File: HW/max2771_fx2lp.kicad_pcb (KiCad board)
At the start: 4 copper layers, 30.7 x 34.2 mm, 70 parts, among them J1 SMA-ANG, J2 SMA-ANG, J3 Screw_Terminal_01x02, J4 SMA-ANG, J5 Conn_01x05_Pin, P1 Conn_02x10_Odd_Even, P2 Conn_02x10_Odd_Even, U1 MAX2771, U2 MAX2771

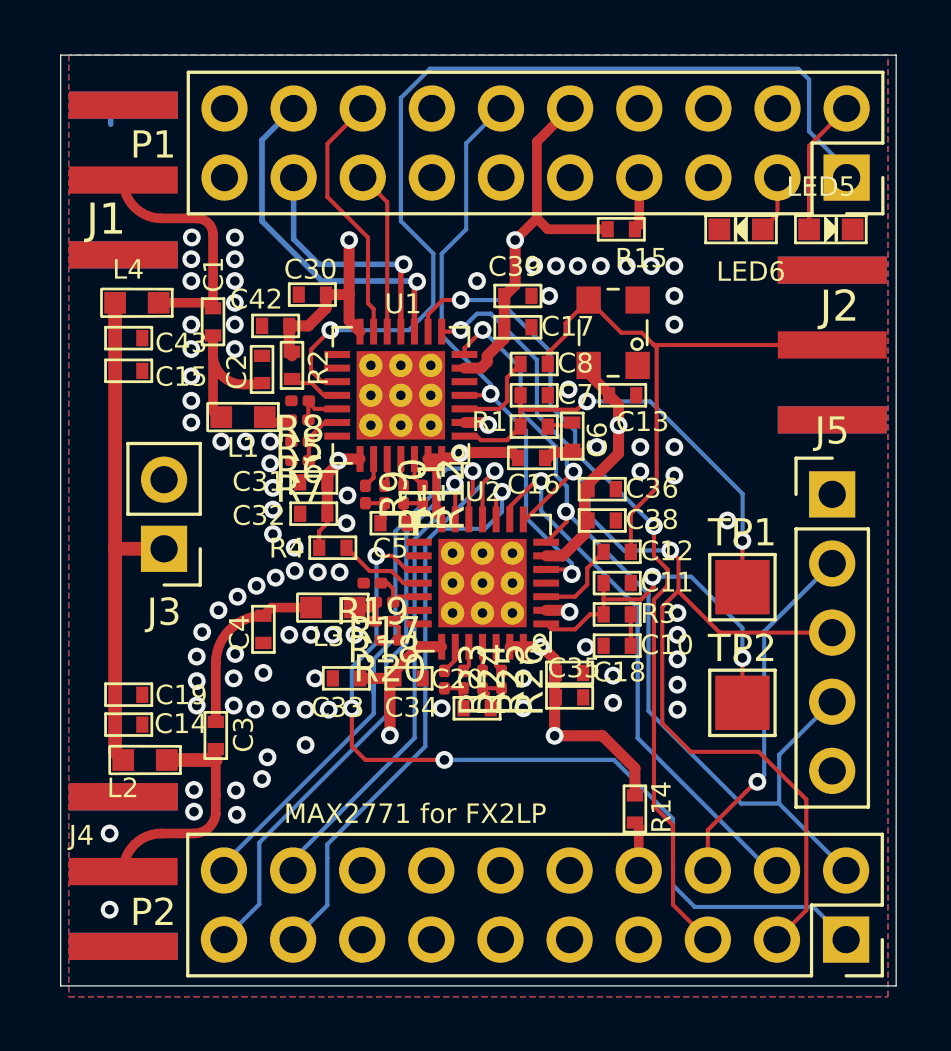
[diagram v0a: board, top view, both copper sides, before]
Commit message: mirror connectors
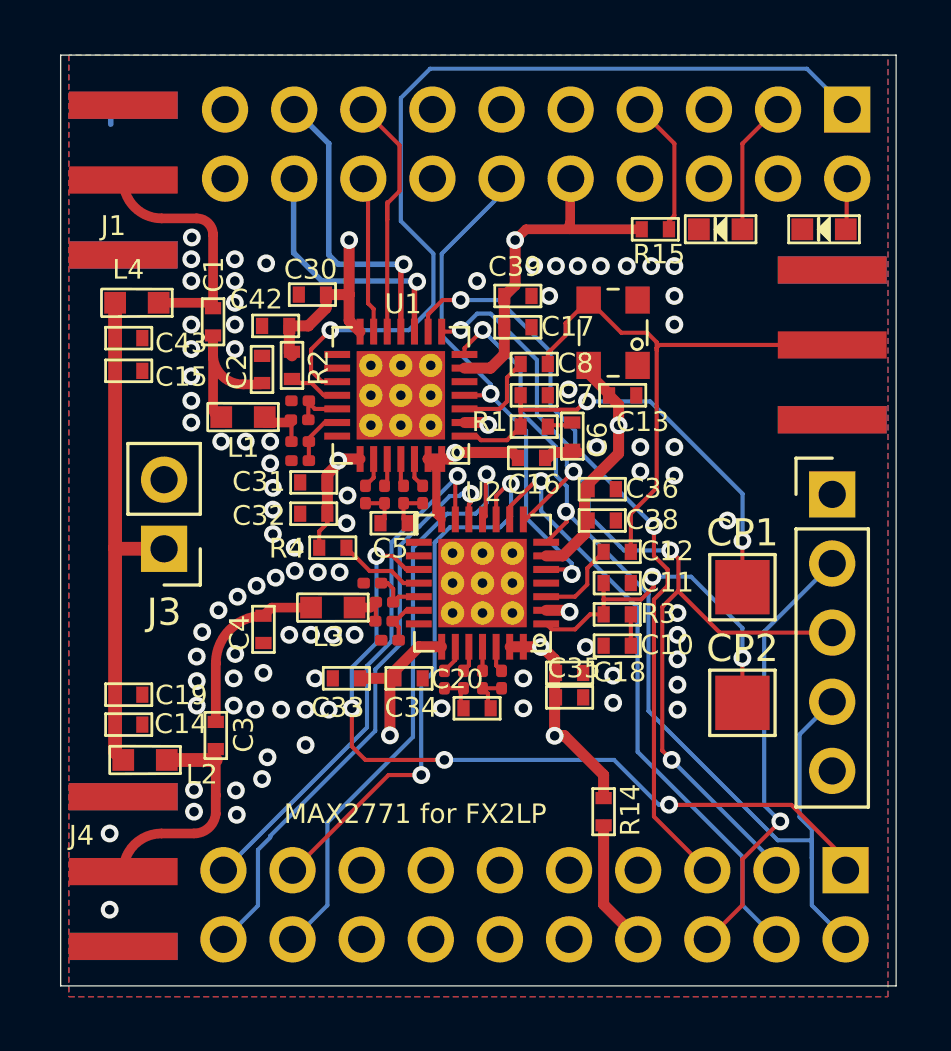
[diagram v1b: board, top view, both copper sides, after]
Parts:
- removed TP1, TP2: TestPoint, TestPoint:TestPoint_Pad_2.0x2.0mm
- added CP1: TestPoint, TestPoint:TestPoint_Pad_2.0x2.0mm, F.Cu at (151.0, 109.6)
- added CP2: TestPoint, TestPoint:TestPoint_Pad_2.0x2.0mm, F.Cu at (151.0, 113.8)
- P1, P2: moved to B.Cu
- moved P2 2.55 mm to (154.7, 120.0), turned to 90 degrees
- moved P1 2.50 mm to (154.8, 92.0), turned to 90 degrees
- moved R15 1.25 mm to (147.8, 96.5)
- moved R14 1.15 mm to (145.9, 117.8)
- moved LED6 0.75 mm to (150.2, 96.5)
- moved LED5 0.25 mm to (154.0, 96.5), turned to 180 degrees
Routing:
- net +3.3V: track 129.3 -> 124.1 mm
- net SCLK: track 42.3 -> 37.8 mm, vias 3 -> 4
- net SDATA: track 33.4 -> 37.7 mm
- net I1_A: track 9.44 -> 5.83 mm
- net I0_A: track 6.03 -> 9.60 mm
- net Q1_A: track 13.1 -> 9.62 mm
- net /SLRD: track 1.97 -> 5.06 mm
- net PA7: track 13.3 -> 16.2 mm
- net /PA5: track 1.82 -> 4.73 mm
- net PD7: track 2.12 -> 4.97 mm
- net /PD6: track 5.01 -> 2.23 mm
- net CSN_A: track 30.7 -> 28.0 mm
- net CSN_B: track 19.8 -> 22.4 mm
- net DCLK: track 22.3 -> 19.7 mm
- net Q0_B: track 20.0 -> 22.4 mm
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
